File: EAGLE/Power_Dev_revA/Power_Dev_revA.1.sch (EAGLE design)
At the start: 36 parts, among them J5 MICRO_USB_SMD, Q1 SI2301CDS-T1-GE3, Q2 SI2301CDS-T1-GE3, U1 CN3791, U3 DW01A-G, U4 FS8205A

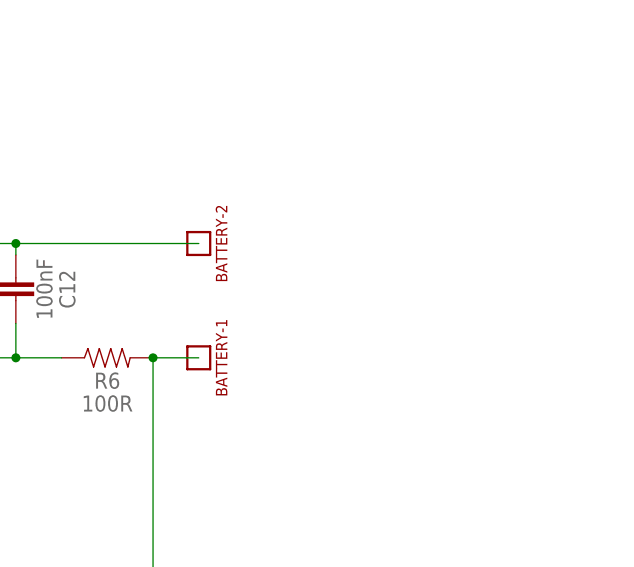
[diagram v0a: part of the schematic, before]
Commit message: Power A.2
Added connector for battery
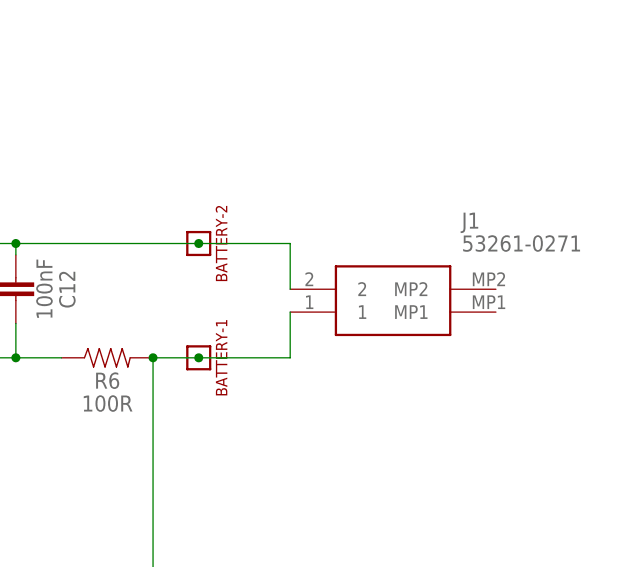
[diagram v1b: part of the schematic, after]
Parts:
- added J1: 53261-0271, NSE LABS:53261-0271
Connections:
- net N$18: now also J1.2
- net N$20: now also J1.1
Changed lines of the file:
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@@
 <part name="OUTPUT" library="NSE LABS" deviceset="HEADER_2PIN" device=""/>
 <part name="SUPPLY20" library="supply2" library_urn="urn:adsk.eagle:library:372" deviceset="GND" device=""/>
+<part name="J1" library="NSE LABS" deviceset="53261-0271" device=""/>
 </parts>
 <sheets>
@@
 <instance part="OUTPUT" gate="-2" x="208.28" y="38.1" rot="R180"/>
 <instance part="SUPPLY20" gate="GND" x="208.28" y="30.48"/>
+<instance part="J1" gate="G$1" x="243.84" y="17.78"/>
 </instances>
 <busses>
@@
 <wire x1="233.68" y1="22.86" x2="213.36" y2="22.86" width="0.1524" layer="91"/>
 <junction x="213.36" y="22.86"/>
+<pinref part="J1" gate="G$1" pin="2"/>
+<wire x1="243.84" y1="17.78" x2="243.84" y2="22.86" width="0.1524" layer="91"/>
+<wire x1="243.84" y1="22.86" x2="233.68" y2="22.86" width="0.1524" layer="91"/>
+<junction x="233.68" y="22.86"/>
 </segment>
 </net>
@@
 <junction x="99.06" y="15.24"/>
 <wire x1="124.46" y1="15.24" x2="114.3" y2="15.24" width="0.1524" layer="91"/>
-</segment>
-</net>
+<pinref part="J1" gate="G$1" pin="1"/>
+<wire x1="243.84" y1="15.24" x2="243.84" y2="10.16" width="0.1524" layer="91"/>
+<wire x1="243.84" y1="10.16" x2="233.68" y2="10.16" width="0.1524" layer="91"/>
+<junction x="233.68" y="10.16"/>
+</segment>
+</net>
